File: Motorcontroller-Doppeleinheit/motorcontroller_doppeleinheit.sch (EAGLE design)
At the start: 24 parts, among them Q1 16,384Mhz

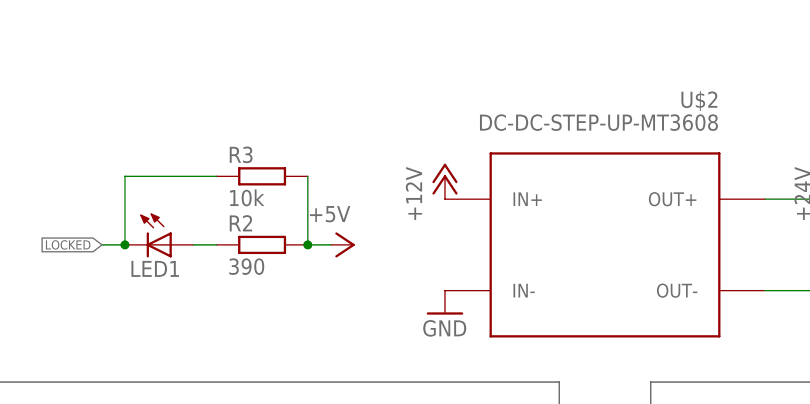
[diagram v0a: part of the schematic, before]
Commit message: Added R4 for current limit if powering on
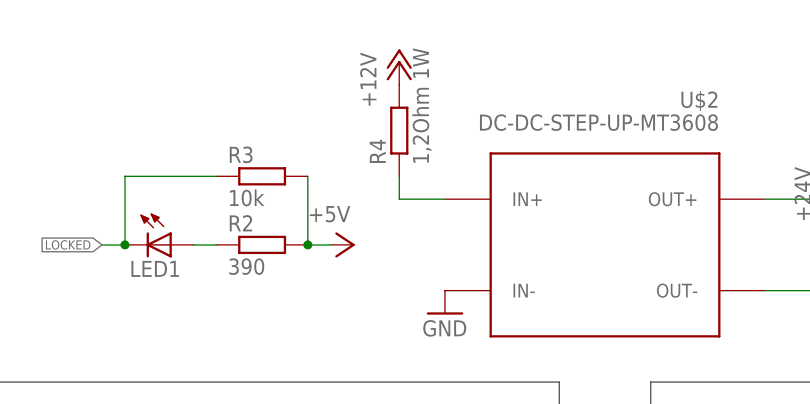
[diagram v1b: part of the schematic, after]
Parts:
- added R4: 1,2Ohm 1W, rcl:R-EU_0411/15
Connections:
- new net N$6: R4.1, U$2.IN+
- net +12V: now also R4.2; no longer U$2.IN+
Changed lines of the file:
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@@
 <part name="C5" library="rcl" deviceset="C-EU" device="C1206" value="1n"/>
 <part name="GND3" library="supply1" deviceset="GND" device=""/>
+<part name="R4" library="rcl" deviceset="R-EU_" device="0411/15" value="1,2Ohm 1W"/>
 </parts>
 <sheets>
@@
 <instance part="GND13" gate="1" x="226.06" y="86.36" rot="R180"/>
 <instance part="GND14" gate="1" x="203.2" y="66.04"/>
-<instance part="P+4" gate="1" x="175.26" y="157.48"/>
+<instance part="P+4" gate="1" x="170.18" y="170.18"/>
 <instance part="GND4" gate="1" x="175.26" y="142.24"/>
 <instance part="Q1" gate="G$1" x="132.08" y="91.44" rot="R90"/>
@@
 </instance>
 <instance part="GND3" gate="1" x="185.42" y="111.76" rot="R180"/>
+<instance part="R4" gate="G$1" x="170.18" y="162.56" rot="R90"/>
 </instances>
 <busses>
@@
 </segment>
 <segment>
-<pinref part="U$2" gate="G$1" pin="IN+"/>
 <pinref part="P+4" gate="1" pin="+12V"/>
+<pinref part="R4" gate="G$1" pin="2"/>
 </segment>
 </net>
@@
 </segment>
 </net>
+<net name="N$6" class="0">
+<segment>
+<pinref part="U$2" gate="G$1" pin="IN+"/>
+<pinref part="R4" gate="G$1" pin="1"/>
+<wire x1="175.26" y1="154.94" x2="170.18" y2="154.94" width="0.1524" layer="91"/>
+<wire x1="170.18" y1="154.94" x2="170.18" y2="157.48" width="0.1524" layer="91"/>
+</segment>
+</net>
